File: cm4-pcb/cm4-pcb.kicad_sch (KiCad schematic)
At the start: 30 parts, among them J1 Conn_01x02_Pin, J2 Conn_01x02_Pin, J3 USB1125-GF-B, J4 Conn_02x03_Odd_Even, U1 Pfostenstecker_6_2x3, U2 Pfostenstecker_6_2x3, U4 MagJack-A70-112-331N126, U5 SMD-PUSH-BTN

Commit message: Added TVS Diodes
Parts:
- removed H1, H2: Pinhead_1x04V, BohleBots:HDR-TH_4P-P2.54-V-M-1, symbol bohlebots.lib:Pinhead_1x04V
- added J5, J6: Conn_01x04, Connector_PinSocket_2.54mm:PinSocket_1x04_P2.54mm_Vertical, symbol Connector_Generic:Conn_01x04
- added U3, U6, U7: TPD4EUSB30, Package_SON:USON-10_2.5x1.0mm_P0.5mm, symbol CM4IO:TPD4EUSB30
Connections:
- net GND: now also U3.3 (GND), U3.8 (GND), U6.3 (GND), U6.8 (GND), U7.3 (GND), U7.8 (GND)
- net P12: now also J5.1 (Pin_1)
- net P13: now also J5.2 (Pin_2)
- net P14: now also J5.3 (Pin_3)
- net P15: now also J5.4 (Pin_4)
- net SCL: now also U7.5 (D2-), U7.6
- net SDA: now also U7.4 (D2+), U7.7
- net TR0_TAP: now also J6.1 (Pin_1)
- net TR1_TAP: now also J6.2 (Pin_2)
- net TR2_TAP: now also J6.3 (Pin_3)
- net TR3_TAP: now also J6.4 (Pin_4)
- net TRD0_N: now also U3.2 (D1-), U3.9
- net TRD0_P: now also U3.1 (D1+), U3.10
- net TRD1_N: now also U3.5 (D2-), U3.6
- net TRD1_P: now also U3.4 (D2+), U3.7
- net TRD2_N: now also U6.2 (D1-), U6.9
- net TRD2_P: now also U6.1 (D1+), U6.10
- net TRD3_N: now also U6.5 (D2-), U6.6
- net TRD3_P: now also U6.4 (D2+), U6.7
- net USB_D+: now also U7.1 (D1+), U7.10
- net USB_D-: now also U7.2 (D1-), U7.9
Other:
- note added: "ESD Protection TVS Diode"
- note added: "Ethernet"
- note added: "USB + I2C"
- moved on the sheet: J3

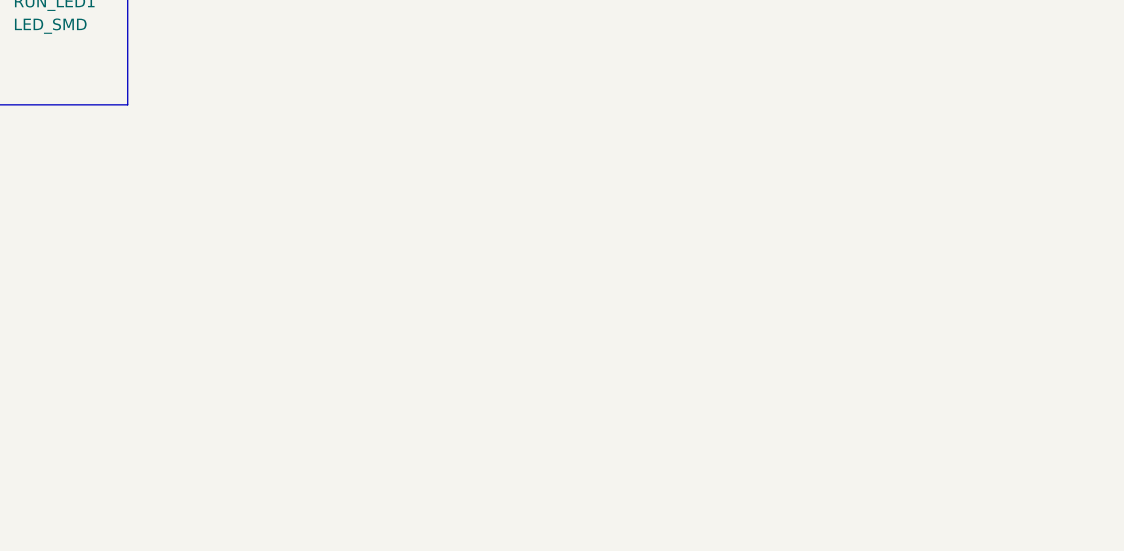
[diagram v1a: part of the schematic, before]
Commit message: Added +5V Capacitors
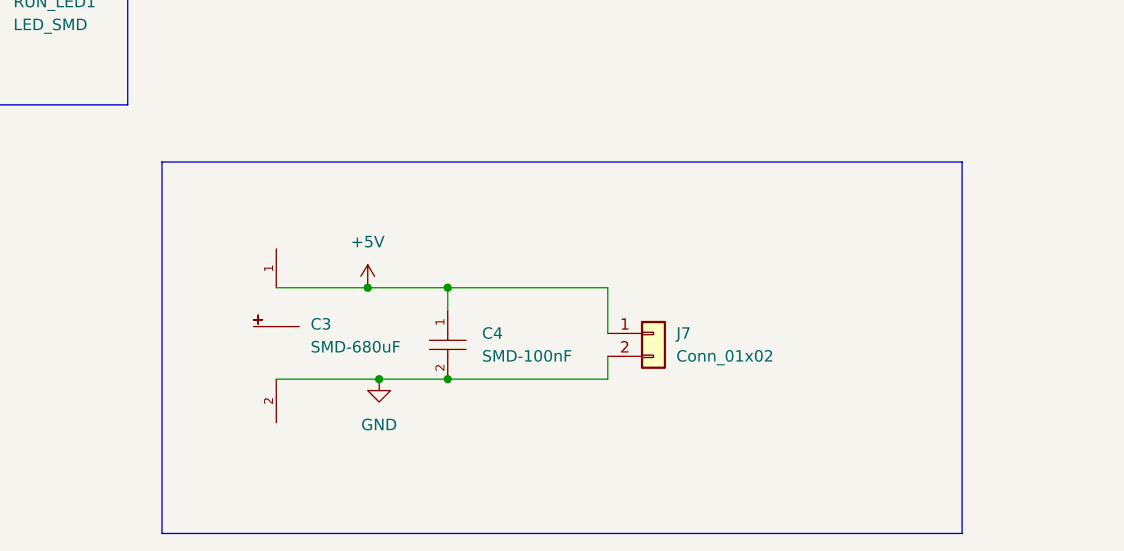
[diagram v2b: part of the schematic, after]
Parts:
- added C3: SMD-680uF, BohleBots:CAP-SMD_BD10.0-L10.3-W10.3-LS11.3-FD, symbol bohlebots.lib:SMD-680uF
- added C4: SMD-100nF, BohleBots:C0603, symbol bohlebots.lib:SMD-100nF
- added J7: Conn_01x02, Connector_PinHeader_2.54mm:PinHeader_1x02_P2.54mm_Vertical, symbol Connector_Generic:Conn_01x02
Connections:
- net +5V: now also C3.1, C4.1, J7.1 (Pin_1)
- net GND: now also C3.2, C4.2, J7.2 (Pin_2)

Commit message: Changed Ethernet Magjack + some layout changes
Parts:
- removed J6: Conn_01x04, Connector_PinSocket_2.54mm:PinSocket_1x04_P2.54mm_Vertical, symbol Connector_Generic:Conn_01x04
- removed R7, R8: SMD-470R, BohleBots:R0603, symbol bohlebots.lib:SMD-470R
- removed U4: MagJack-A70-112-331N126, CM4IO:TRJG0926HENL, symbol CM4IO:MagJack-A70-112-331N126
- removed U6: TPD4EUSB30, Package_SON:USON-10_2.5x1.0mm_P0.5mm, symbol CM4IO:TPD4EUSB30
- added J6: J0011D21NL, J0011D21NL, symbol J0011D21NL:J0011D21NL
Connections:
- net GND: now also J6.8 (CHS_GROUND), J6.MH1, J6.MH2
- net TRD0_N: now also J6.2 (TD-)
- net TRD0_P: now also J6.1 (TD+)
- net TRD1_N: now also J6.6 (RD-)
- net TRD1_P: now also J6.3 (RD+)
- net at C1.2: now also J6.4 (CT_1), J6.5 (CT_2)
- net ETH_LEDG: no longer names the net of Module1.17 (Ethernet_nLED2(3.3v))
- net ETH_LEDY: no longer names the net of Module1.15 (Ethernet_nLED3(3.3v))
- net TRD2_N: no longer names the net of Module1.9 (Ethernet_Pair2_N)
- net TRD2_P: no longer names the net of Module1.11 (Ethernet_Pair2_P)
- net TRD3_N: no longer names the net of Module1.5 (Ethernet_Pair3_N)
- net TRD3_P: no longer names the net of Module1.3 (Ethernet_Pair3_P)
- no-connect marks 120 -> 126
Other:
- note added: "Ethernet Magjack"
- note removed: "Ethernet Tap"
- note removed: "RJ45 Connector"
- moved on the sheet: J3, U3, U7

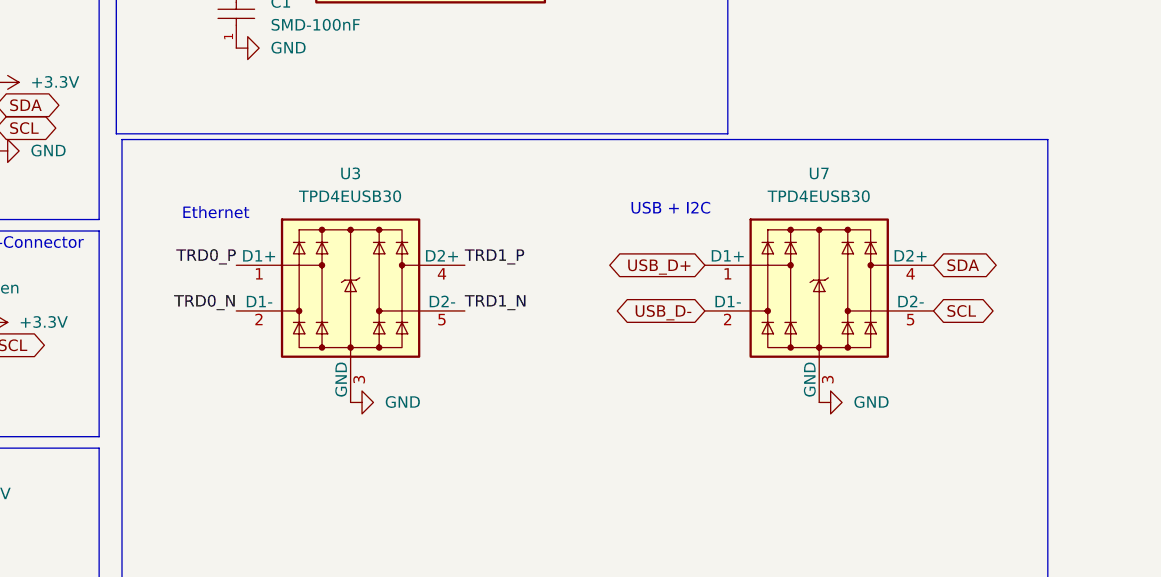
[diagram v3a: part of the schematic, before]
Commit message: Remove ESD Diodes
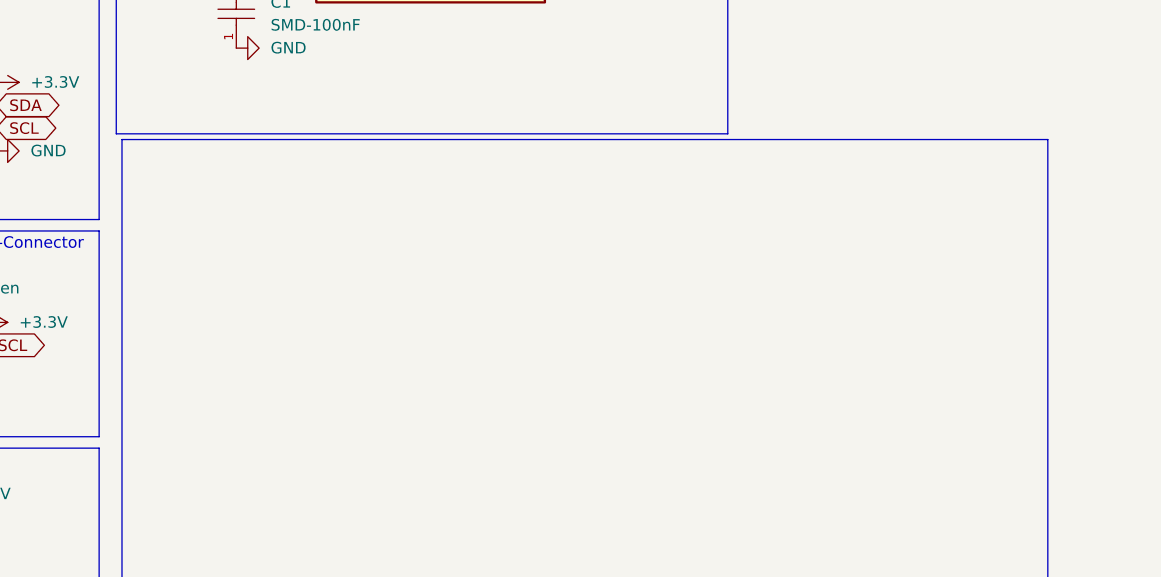
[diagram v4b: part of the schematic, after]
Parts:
- removed U3, U7: TPD4EUSB30, Package_SON:USON-10_2.5x1.0mm_P0.5mm, symbol CM4IO:TPD4EUSB30
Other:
- note removed: "Ethernet"
- note removed: "USB + I2C"

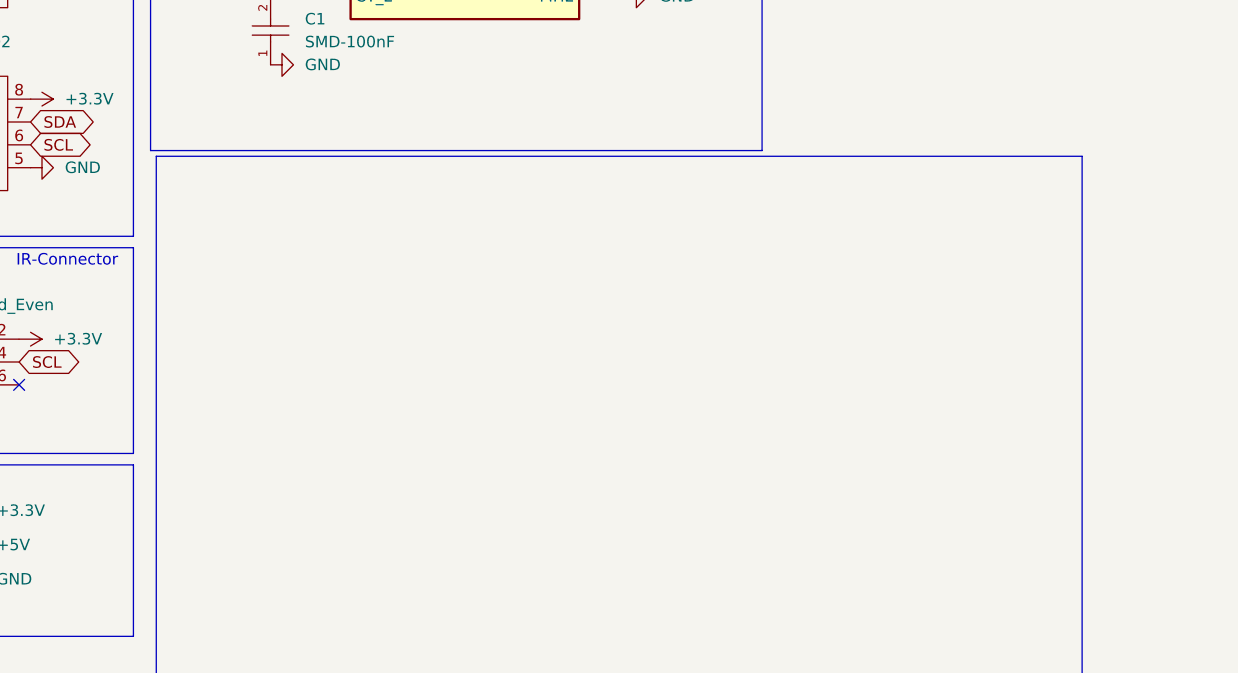
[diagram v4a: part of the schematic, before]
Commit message: Changed TVS Diodes
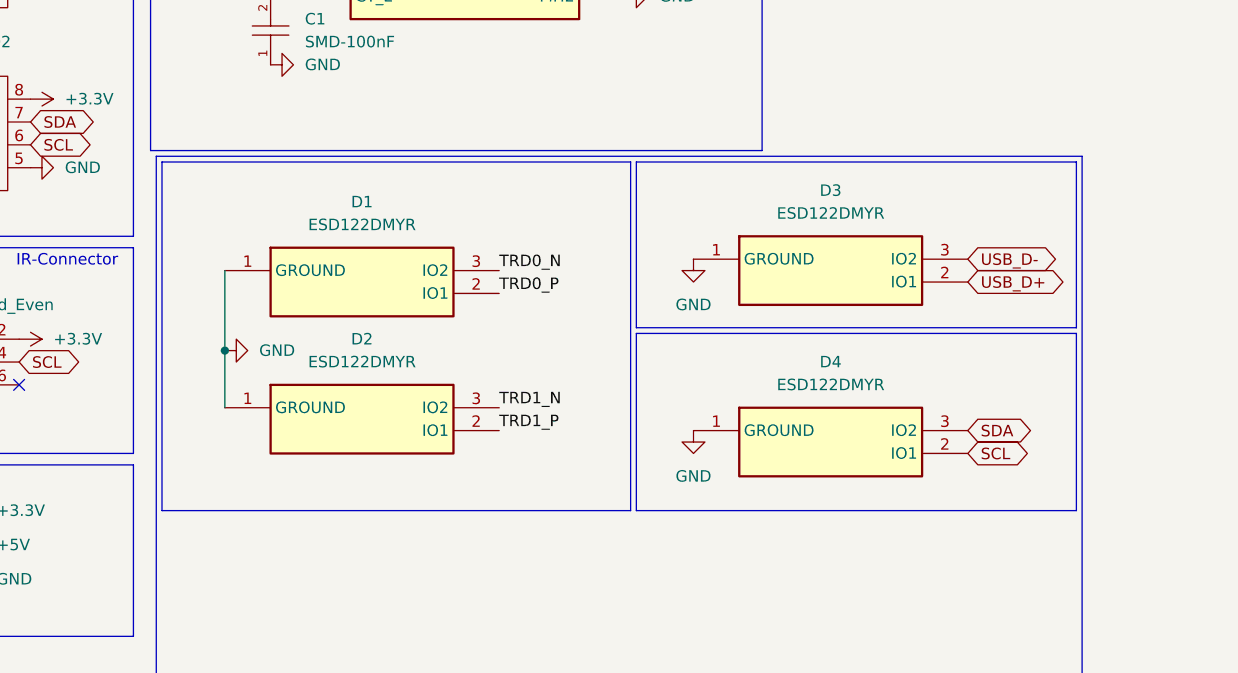
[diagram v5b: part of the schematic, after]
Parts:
- added D1, D2, D3, D4: ESD122DMYR, ESD122DMYR, symbol ESD122DMYR:ESD122DMYR
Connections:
- net GND: now also D1.1 (GROUND), D2.1 (GROUND), D3.1 (GROUND), D4.1 (GROUND)
- net SCL: now also D4.2 (IO1)
- net SDA: now also D4.3 (IO2)
- net TRD0_N: now also D1.3 (IO2)
- net TRD0_P: now also D1.2 (IO1)
- net TRD1_N: now also D2.3 (IO2)
- net TRD1_P: now also D2.2 (IO1)
- net USB_D+: now also D3.2 (IO1)
- net USB_D-: now also D3.3 (IO2)
